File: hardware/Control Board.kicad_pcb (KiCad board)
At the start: 2 copper layers, 68.4 x 51.5 mm, 54 parts, among them J1 SOLAR, J2 Conn_FTDI, M1 MOTOR, Q1 BC817W, Q2 IRF7105PbF, Q3 BC817W, Q4 BC817W, Q5 IRF7105PbF, Q6 BC817W, SW1 PROG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

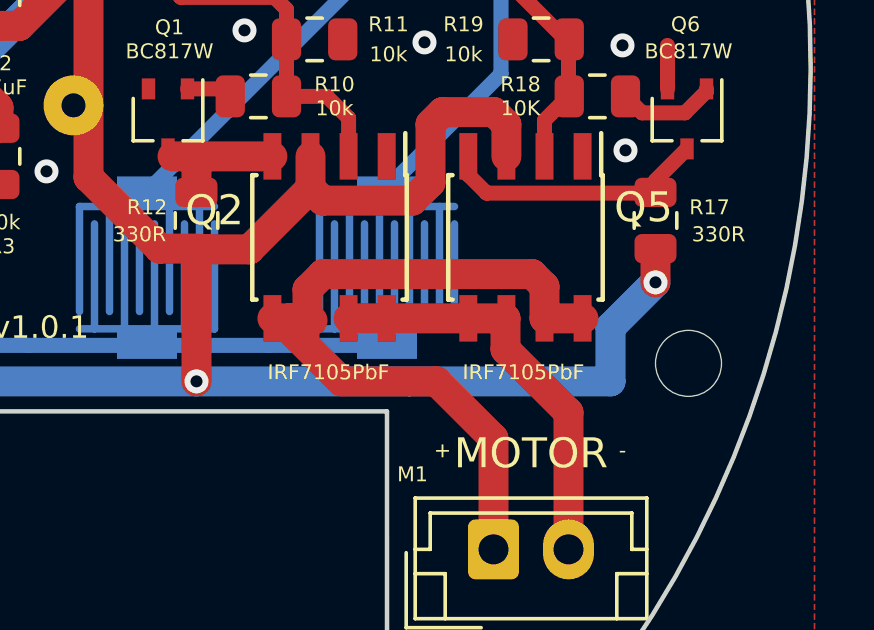
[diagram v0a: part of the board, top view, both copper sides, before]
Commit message: Moving batt via away from the screw head
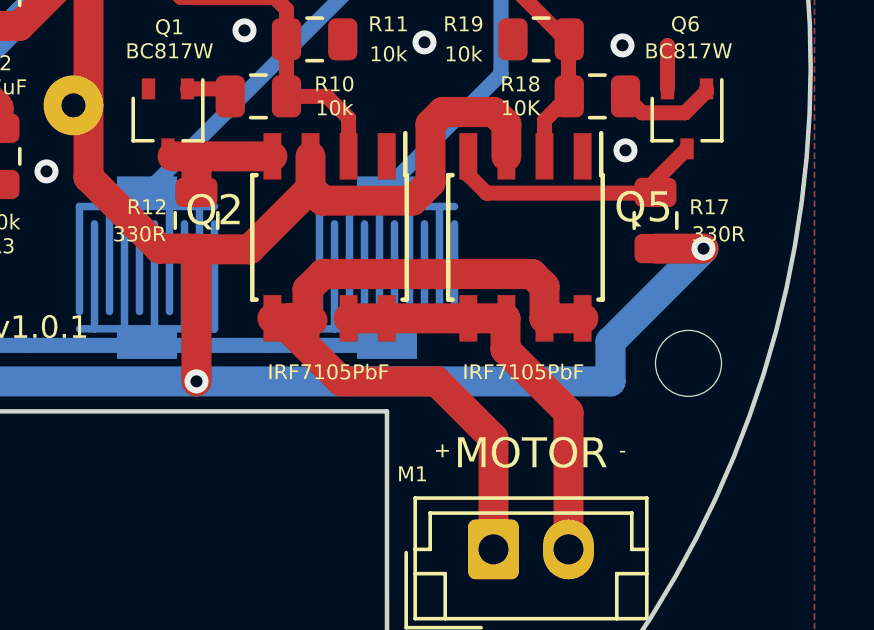
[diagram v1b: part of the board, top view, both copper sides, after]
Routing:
- net +BATT: track 124.0 -> 126.3 mm
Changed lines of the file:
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@@
     (thickness 1.6)
     (drawings 57)
-    (tracks 335)
+    (tracks 334)
     (zones 0)
     (modules 54)
@@
   (segment (start 122.9 141) (end 86.7 141) (width 1) (layer B.Cu) (net 2))
   (via (at 122.9 141) (size 0.8) (drill 0.4) (layers F.Cu B.Cu) (net 2))
-  (segment (start 130 141) (end 122.9 141) (width 1) (layer B.Cu) (net 2))
   (segment (start 117 129.15) (end 119.3 126.85) (width 1) (layer F.Cu) (net 2))
   (segment (start 116.3 129.15) (end 117 129.15) (width 1) (layer F.Cu) (net 2))
@@
   (segment (start 119.3 126.85) (end 119.3 126.2) (width 1) (layer F.Cu) (net 2))
   (via (at 119.3 126.2) (size 0.8) (drill 0.4) (layers F.Cu B.Cu) (net 2))
-  (via (at 138.2 137.7) (size 0.8) (drill 0.4) (layers F.Cu B.Cu) (net 2))
-  (segment (start 136.7 139.2) (end 136.7 141) (width 1) (layer B.Cu) (net 2))
-  (segment (start 138.2 137.7) (end 136.7 139.2) (width 1) (layer B.Cu) (net 2))
-  (segment (start 136.7 141) (end 130 141) (width 1) (layer B.Cu) (net 2))
-  (segment (start 138.2 137.7) (end 138.2 136.6) (width 1) (layer F.Cu) (net 2))
+  (via (at 139.8 136.575) (size 0.8) (drill 0.4) (layers F.Cu B.Cu) (net 2))
   (segment (start 124.665002 136.6) (end 126.7 134.565002) (width 1) (layer F.Cu) (net 2))
   (segment (start 122.9 136.6) (end 124.665002 136.6) (width 1) (layer F.Cu) (net 2))
@@
   (segment (start 121.675 136.575) (end 119.3 134.2) (width 1) (layer F.Cu) (net 2))
   (segment (start 119.3 126.2) (end 119.3 134.2) (width 1) (layer F.Cu) (net 2))
+  (segment (start 138.2 136.575) (end 139.8 136.575) (width 1) (layer F.Cu) (net 2))
+  (segment (start 136.7 141) (end 136.7 139.675) (width 1) (layer B.Cu) (net 2))
+  (segment (start 136.7 139.675) (end 139.8 136.575) (width 1) (layer B.Cu) (net 2))
+  (segment (start 122.9 141) (end 136.7 141) (width 1) (layer B.Cu) (net 2))
   (via (at 136.1 119.463749) (size 0.8) (drill 0.4) (layers F.Cu B.Cu) (net 3))
   (segment (start 96.1 123.75) (end 96.1 123.239998) (width 0.5) (layer F.Cu) (net 3))
